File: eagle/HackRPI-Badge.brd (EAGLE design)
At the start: 124.5 x 94 mm, 43 parts, among them J1 FTDI_BASICPTH, J2 SOLDERJUMPERTRACE-PTH, U2 3.3V, U4 74595, U5 74595, U6 74595, U7 74165DT

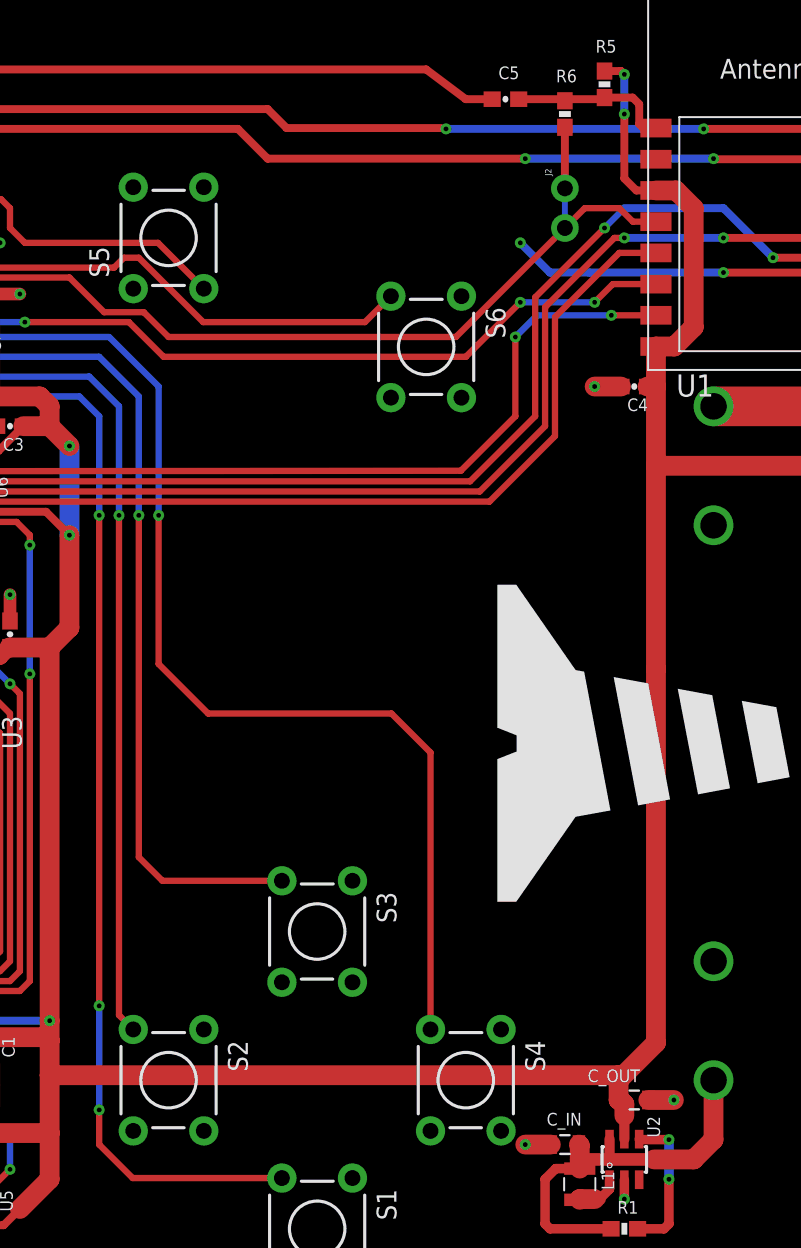
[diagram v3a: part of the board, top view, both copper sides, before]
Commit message: Tied GPIO0 to DTR, changed deep sleep jumper to normally open (necessary for programming)
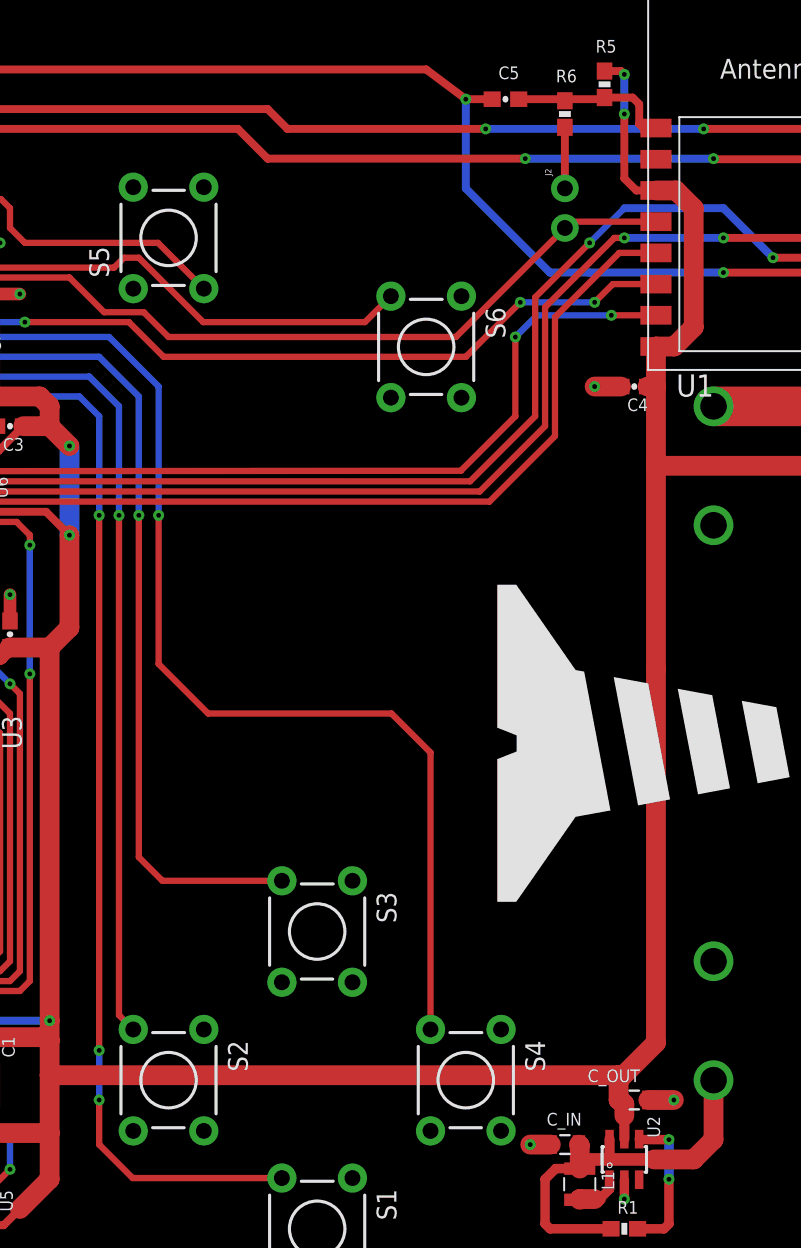
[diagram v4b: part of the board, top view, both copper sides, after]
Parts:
- J2: value SOLDERJUMPERTRACE-PTH -> SOLDERJUMPERPTH; device SparkFun-Retired:SJ_2S-TRACE-PTH -> SparkFun-Retired:SJ_2S-PTH
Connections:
- removed net GPIO0: R3.1, U1.12
- net DTR: now also R3.1, U1.12
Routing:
- net DTR: track 57.9 -> 98.3 mm, vias 0 -> 2
- net GPIO0: track 29.8 -> 0.00 mm, vias 2 -> 0
- net INPUT_CS: track 52.3 -> 51.6 mm
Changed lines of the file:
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@@
 <attribute name="VALUE" x="91.821" y="88.138" size="0.4064" layer="27" font="vector" rot="R180"/>
 </element>
-<element name="J2" library="SparkFun-Retired" package="SJ_2S-TRACE-PTH" value="SOLDERJUMPERTRACE-PTH" x="94.615" y="80.01" rot="R270"/>
+<element name="J2" library="SparkFun-Retired" package="SJ_2S-PTH" value="SOLDERJUMPERPTH" x="94.615" y="80.01" rot="R270"/>
 <element name="U7" library="mylib" package="TSSOP16" value="74165DT" x="53.975" y="76.2" smashed="yes" rot="R180">
 <attribute name="NAME" x="57.4675" y="76.7715" size="0.8128" layer="25" rot="R270"/>
@@
 <via x="48.26" y="53.34" extent="1-16" drill="0.3048"/>
 <wire x1="99.96" y1="22.86" x2="101.6" y2="22.86" width="1.27" layer="1"/>
-<wire x1="93.715" y1="20.0025" x2="92.075" y2="20.0025" width="1.27" layer="1"/>
-<via x="92.075" y="20.0025" extent="1-16" drill="0.3048"/>
+<wire x1="93.715" y1="20.0025" x2="92.3925" y2="20.0025" width="1.27" layer="1"/>
+<via x="92.3925" y="20.0025" extent="1-16" drill="0.3048"/>
 </signal>
 <signal name="INPUT_CS">
@@
 <contactref element="U1" pad="4"/>
 <contactref element="J2" pad="2"/>
-<wire x1="94.615" y1="78.74" x2="95.885" y2="80.01" width="0.4064" layer="1"/>
-<wire x1="95.885" y1="80.01" x2="98.1075" y2="80.01" width="0.4064" layer="1"/>
-<wire x1="98.1075" y1="80.01" x2="98.9725" y2="79.145" width="0.4064" layer="1"/>
-<wire x1="98.9725" y1="79.145" x2="100.45" y2="79.145" width="0.4064" layer="1"/>
 <wire x1="87.63" y1="71.755" x2="94.615" y2="78.74" width="0.4064" layer="1"/>
-</signal>
-<signal name="GPIO0">
-<contactref element="U1" pad="12"/>
-<contactref element="R3" pad="1"/>
-<via x="91.7575" y="77.7875" extent="1-16" drill="0.3048"/>
-<wire x1="91.7575" y1="77.7875" x2="93.6625" y2="75.8825" width="0.508" layer="16"/>
-<wire x1="93.6625" y1="75.8825" x2="96.2025" y2="75.8825" width="0.508" layer="16"/>
-<via x="104.775" y="75.8825" extent="1-16" drill="0.3048"/>
-<wire x1="96.2025" y1="75.8825" x2="104.775" y2="75.8825" width="0.508" layer="16"/>
-<wire x1="104.775" y1="75.8825" x2="112.0775" y2="75.8825" width="0.508" layer="1"/>
-<wire x1="112.0775" y1="75.8825" x2="113.34" y2="77.145" width="0.508" layer="1"/>
-<wire x1="113.34" y1="77.145" x2="115.45" y2="77.145" width="0.508" layer="1"/>
-<wire x1="119.165" y1="77.47" x2="118.84" y2="77.145" width="0.8128" layer="1"/>
-<wire x1="118.84" y1="77.145" x2="115.45" y2="77.145" width="0.8128" layer="1"/>
-<wire x1="95.25" y1="75.8825" x2="96.2025" y2="75.8825" width="0.4064" layer="16"/>
+<wire x1="94.615" y1="78.74" x2="95.02" y2="79.145" width="0.4064" layer="1"/>
+<wire x1="95.02" y1="79.145" x2="100.45" y2="79.145" width="0.4064" layer="1"/>
 </signal>
 <signal name="V_BATT" class="1">
@@
 <wire x1="88.54" y1="62.505" x2="92.71" y2="66.675" width="0.4064" layer="1"/>
 <wire x1="92.71" y1="66.675" x2="92.71" y2="74.295" width="0.4064" layer="1"/>
-<wire x1="92.71" y1="74.295" x2="97.155" y2="78.74" width="0.4064" layer="1"/>
-<via x="97.155" y="78.74" extent="1-16" drill="0.3048"/>
-<wire x1="97.155" y1="78.74" x2="98.425" y2="80.01" width="0.4064" layer="16"/>
+<wire x1="92.71" y1="74.295" x2="96.2025" y2="77.7875" width="0.4064" layer="1"/>
+<via x="96.2025" y="77.7875" extent="1-16" drill="0.3048"/>
+<wire x1="96.2025" y1="77.7875" x2="98.425" y2="80.01" width="0.4064" layer="16"/>
 <wire x1="98.425" y1="80.01" x2="104.775" y2="80.01" width="0.508" layer="16"/>
 <wire x1="104.775" y1="80.01" x2="107.95" y2="76.835" width="0.508" layer="16"/>
@@
 <wire x1="31.75" y1="89.535" x2="34.925" y2="86.36" width="0.508" layer="1"/>
 <wire x1="34.925" y1="86.36" x2="75.565" y2="86.36" width="0.508" layer="1"/>
-<wire x1="75.565" y1="86.36" x2="76.78" y2="85.145" width="0.508" layer="1"/>
+<wire x1="75.565" y1="86.36" x2="76.835" y2="85.09" width="0.508" layer="1"/>
 <wire x1="115.45" y1="85.145" x2="115.395" y2="85.09" width="0.508" layer="1"/>
 <wire x1="115.395" y1="85.09" x2="103.505" y2="85.09" width="0.508" layer="1"/>
 <via x="103.505" y="85.09" extent="1-16" drill="0.3048"/>
-<wire x1="103.505" y1="85.09" x2="86.995" y2="85.09" width="0.508" layer="16"/>
-<via x="86.995" y="85.09" extent="1-16" drill="0.3048"/>
-<wire x1="86.995" y1="85.09" x2="86.94" y2="85.145" width="0.508" layer="1"/>
-<wire x1="86.94" y1="85.145" x2="76.78" y2="85.145" width="0.508" layer="1"/>
+<wire x1="103.505" y1="85.09" x2="89.535" y2="85.09" width="0.508" layer="16"/>
+<via x="89.535" y="85.09" extent="1-16" drill="0.3048"/>
+<wire x1="76.835" y1="85.09" x2="89.535" y2="85.09" width="0.508" layer="1"/>
 </signal>
 <signal name="RXI">
@@
 <wire x1="85.725" y1="88.9" x2="38.1" y2="88.9" width="0.508" layer="1"/>
 <wire x1="38.1" y1="88.9" x2="34.29" y2="92.71" width="0.508" layer="1"/>
+<contactref element="U1" pad="12"/>
+<contactref element="R3" pad="1"/>
+<wire x1="91.7575" y1="77.7875" x2="91.7575" y2="77.7875" width="0" layer="19" extent="1-16"/>
+<wire x1="91.7575" y1="77.7875" x2="93.6625" y2="75.8825" width="0" layer="19" extent="1-16"/>
+<wire x1="93.6625" y1="75.8825" x2="96.2025" y2="75.8825" width="0.508" layer="16"/>
+<via x="104.775" y="75.8825" extent="1-16" drill="0.3048"/>
+<wire x1="96.2025" y1="75.8825" x2="104.775" y2="75.8825" width="0.508" layer="16"/>
+<wire x1="104.775" y1="75.8825" x2="112.0775" y2="75.8825" width="0.508" layer="1"/>
+<wire x1="112.0775" y1="75.8825" x2="113.34" y2="77.145" width="0.508" layer="1"/>
+<wire x1="113.34" y1="77.145" x2="115.45" y2="77.145" width="0.508" layer="1"/>
+<wire x1="119.165" y1="77.47" x2="118.84" y2="77.145" width="0.8128" layer="1"/>
+<wire x1="118.84" y1="77.145" x2="115.45" y2="77.145" width="0.8128" layer="1"/>
+<wire x1="95.25" y1="75.8825" x2="96.2025" y2="75.8825" width="0.4064" layer="16"/>
+<wire x1="93.6625" y1="75.8825" x2="88.265" y2="81.28" width="0.508" layer="16"/>
+<wire x1="88.265" y1="81.28" x2="88.265" y2="86.995" width="0.508" layer="16"/>
+<via x="88.265" y="86.995" extent="1-16" drill="0.3048"/>
 </signal>
 <signal name="N$1">
@@
 <wire x1="64.77" y1="66.675" x2="64.77" y2="60.325" width="0.4064" layer="16"/>
 <via x="64.77" y="60.325" extent="1-16" drill="0.3048"/>
-<wire x1="64.77" y1="60.325" x2="64.77" y2="28.8925" width="0.4064" layer="1"/>
-<via x="64.77" y="28.8925" extent="1-16" drill="0.3048"/>
-<wire x1="64.77" y1="28.8925" x2="64.77" y2="22.225" width="0.4064" layer="16"/>
-<via x="64.77" y="22.225" extent="1-16" drill="0.3048"/>
-<wire x1="64.77" y1="22.225" x2="64.77" y2="20.0025" width="0.4064" layer="1"/>
+<wire x1="64.77" y1="60.325" x2="64.77" y2="26.035" width="0.4064" layer="1"/>
+<via x="64.77" y="26.035" extent="1-16" drill="0.3048"/>
+<wire x1="64.77" y1="26.035" x2="64.77" y2="22.86" width="0.4064" layer="16"/>
+<via x="64.77" y="22.86" extent="1-16" drill="0.3048"/>
+<wire x1="64.77" y1="22.86" x2="64.77" y2="20.0025" width="0.4064" layer="1"/>
 <wire x1="64.77" y1="20.0025" x2="66.9163" y2="17.8562" width="0.4064" layer="1"/>
 <wire x1="66.9163" y1="17.8562" x2="76.4794" y2="17.8562" width="0.4064" layer="1"/>

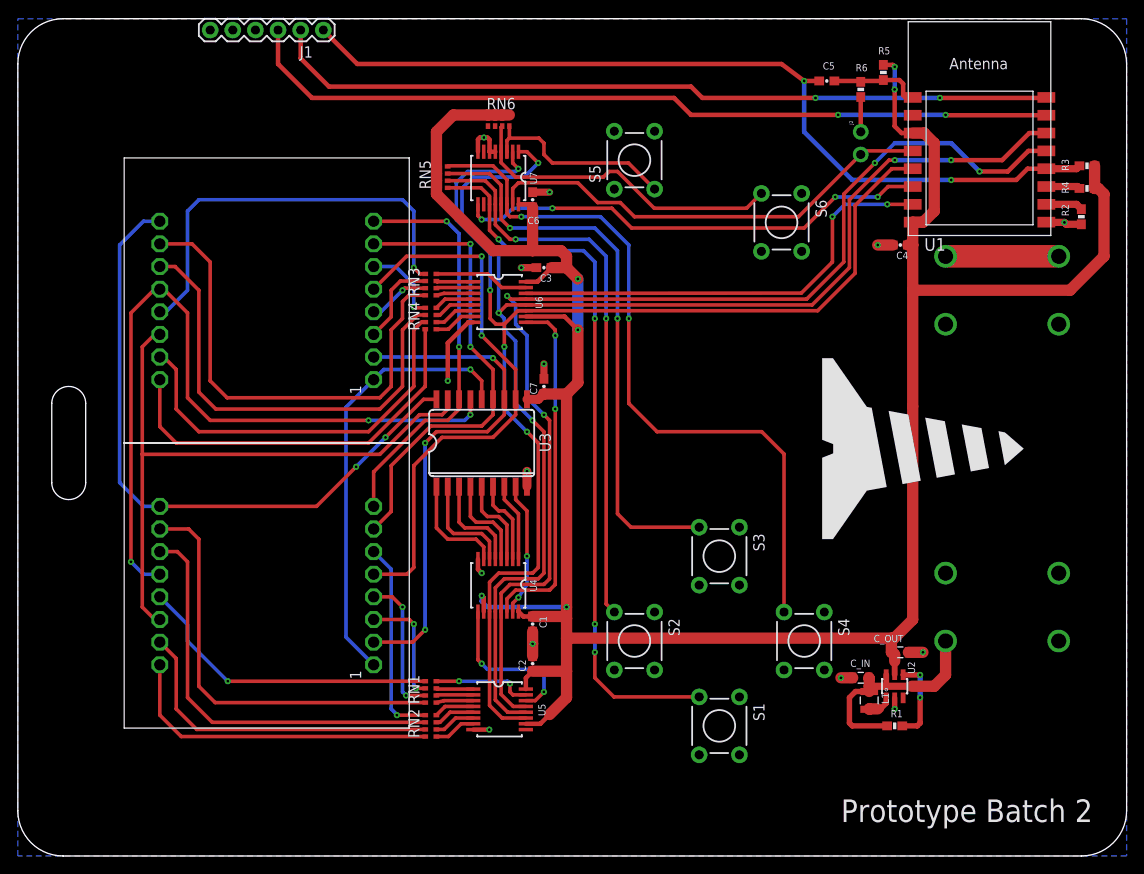
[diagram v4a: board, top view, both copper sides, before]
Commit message: Moved ESP module to center-bottom of badge and made the badge smaller, re-routed traces after resizing badge
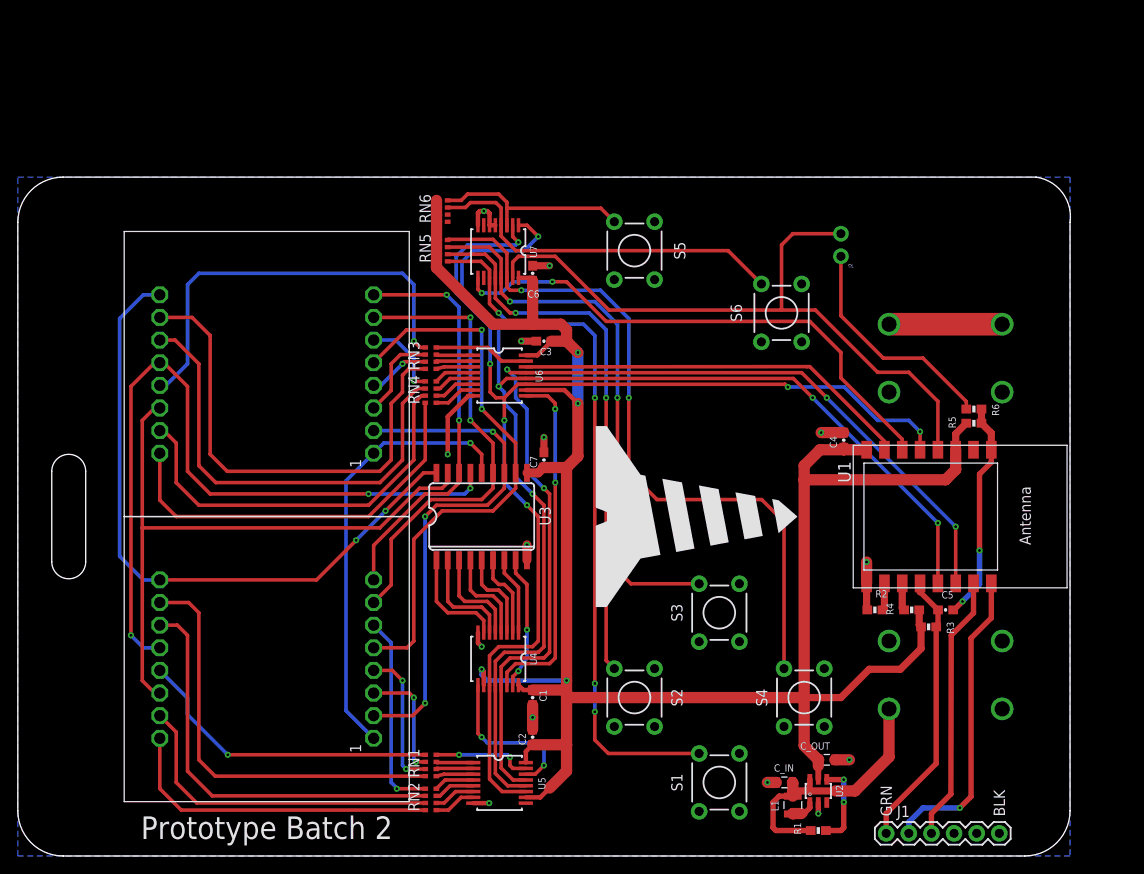
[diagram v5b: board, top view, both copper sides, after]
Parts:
- moved J1 110.1 mm to (97.5, 2.54), turned to 0 degrees
- moved C5 60.9 mm to (104.1, 27.6)
- moved R3 54.7 mm to (102.2, 25.7), turned to 180 degrees
- moved R4 51.2 mm to (100.3, 27.6)
- moved R2 49.8 mm to (96.2, 27.6), turned to 180 degrees
- moved U1 42.7 mm to (104.8, 38.1), turned to 270 degrees
- moved R5 40.7 mm to (107.3, 48.6), turned to 180 degrees
- moved R6 38.1 mm to (107.3, 50.2), turned to 180 degrees
- moved U$2 26.5 mm to (76.2, 38.1)
- moved C4 22.8 mm to (92.7, 46.7), turned to 90 degrees
- moved C_OUT 14.6 mm to (90.8, 10.8)
- moved C_IN 14.5 mm to (86.0, 8.26)
- moved R1 14.5 mm to (89.9, 2.86)
- moved U2 14.5 mm to (89.9, 7.30)
- moved L1 14.5 mm to (87.0, 5.71)
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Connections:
- net LAT: now also U1.13; no longer U1.14
- net OE: now also U1.14; no longer U1.13
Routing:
- net DTR: track 98.3 -> 31.3 mm, vias 2 -> 0
- net RXI: track 92.4 -> 30.0 mm, vias 2 -> 0
- net TXO: track 88.7 -> 34.3 mm, vias 2 -> 1
- net 3.3V: track 284.5 -> 242.3 mm, vias 6 -> 4
- net INPUT_CS: track 51.6 -> 76.4 mm
- net N$1: track 3.91 -> 25.6 mm
- net RESET: track 10.5 -> 24.8 mm, vias 0 -> 2
- net LAT: track 156.5 -> 145.4 mm
- net OE: track 129.2 -> 118.5 mm
- net MISO: track 53.6 -> 59.8 mm, vias 4 -> 2
- net SCK: track 139.6 -> 133.5 mm, vias 4 -> 6
- net MOSI: track 50.5 -> 44.7 mm, vias 2 -> 0
- net V_BATT: track 25.5 -> 30.4 mm
- net B: track 36.7 -> 41.1 mm
- net UP: track 63.8 -> 61.9 mm
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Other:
- board size 124.5 x 94 mm -> 118.2 x 76.2 mm
